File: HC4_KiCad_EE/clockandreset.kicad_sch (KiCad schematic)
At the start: 19 parts, among them IC15 74HC14, SW3 SW_Push, SW4 SW_Push, SW5 SW_SPDT, SW6 SW_SPDT

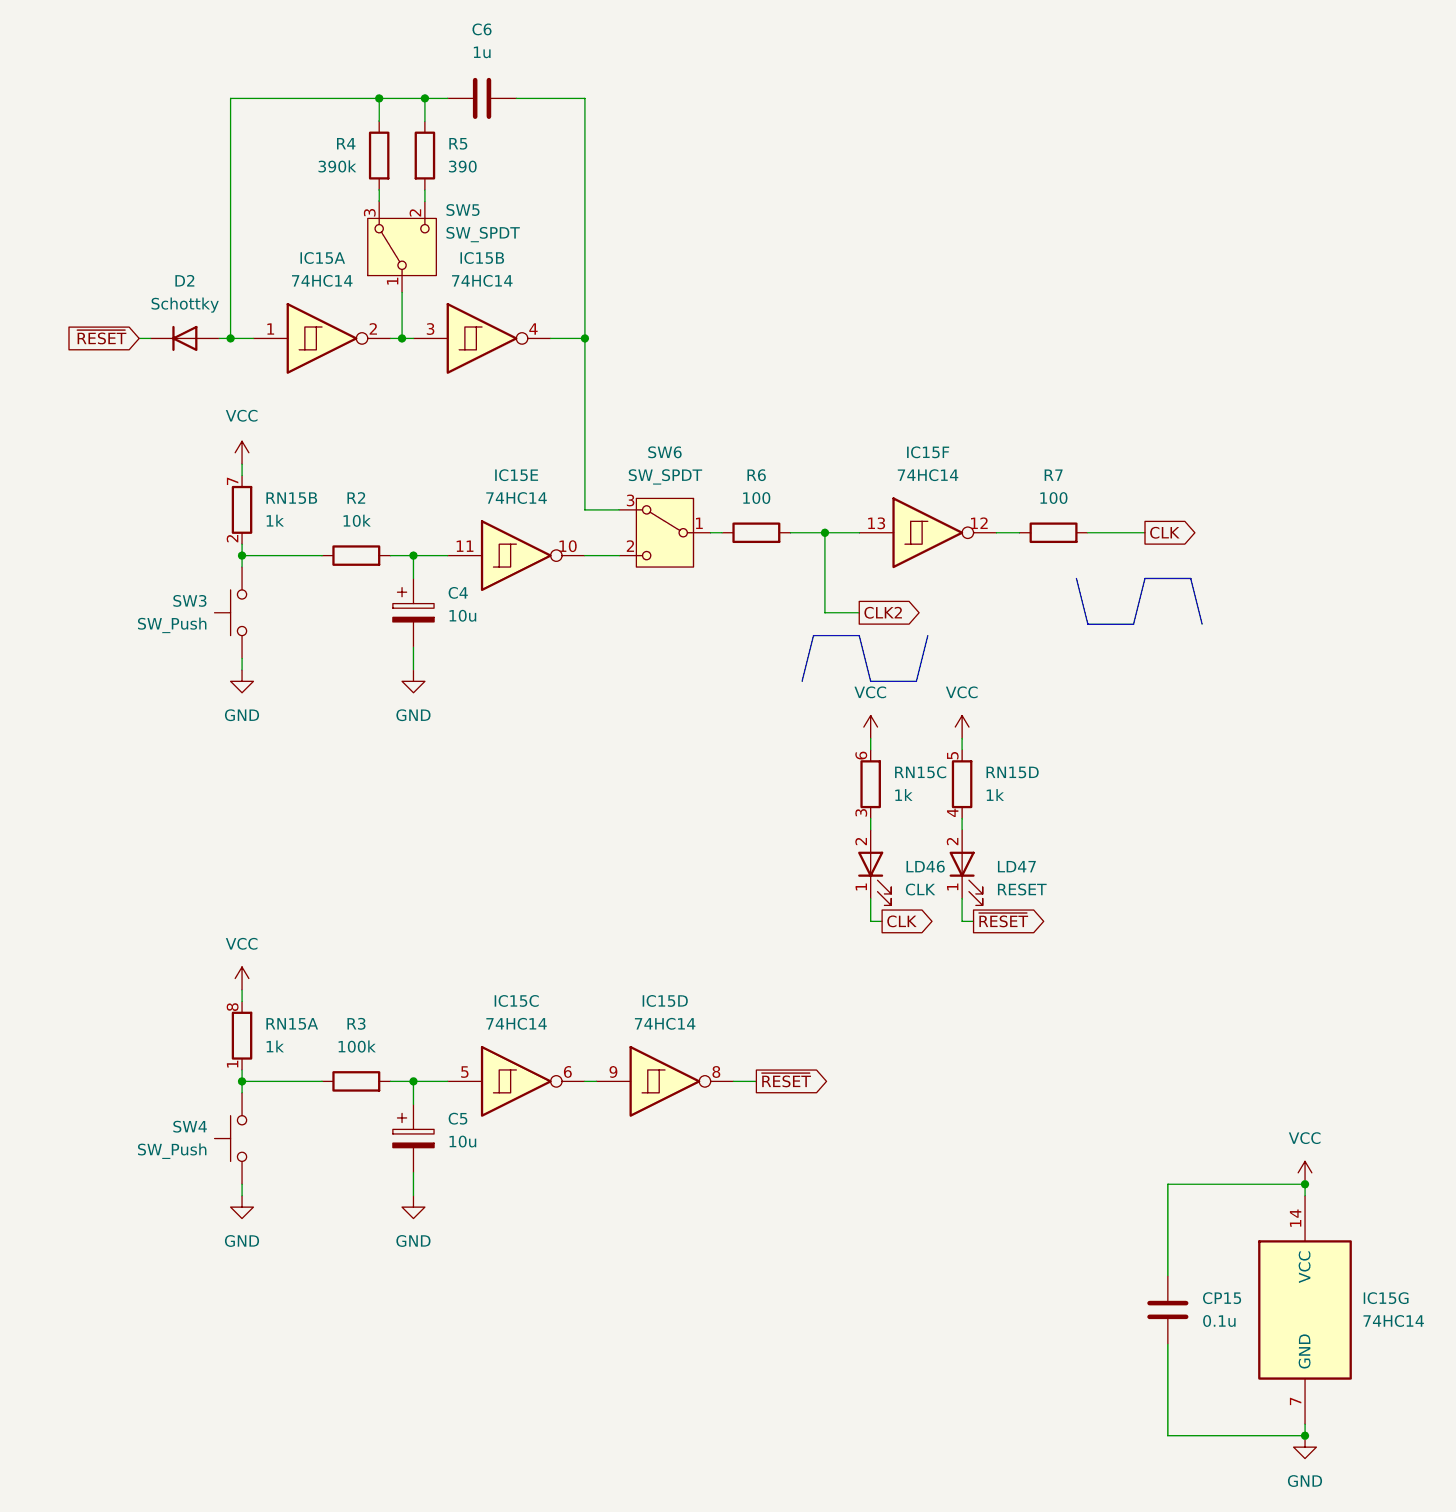
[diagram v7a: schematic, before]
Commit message: 基板を若干改版、フットプリントの指定が外れていたのを修正
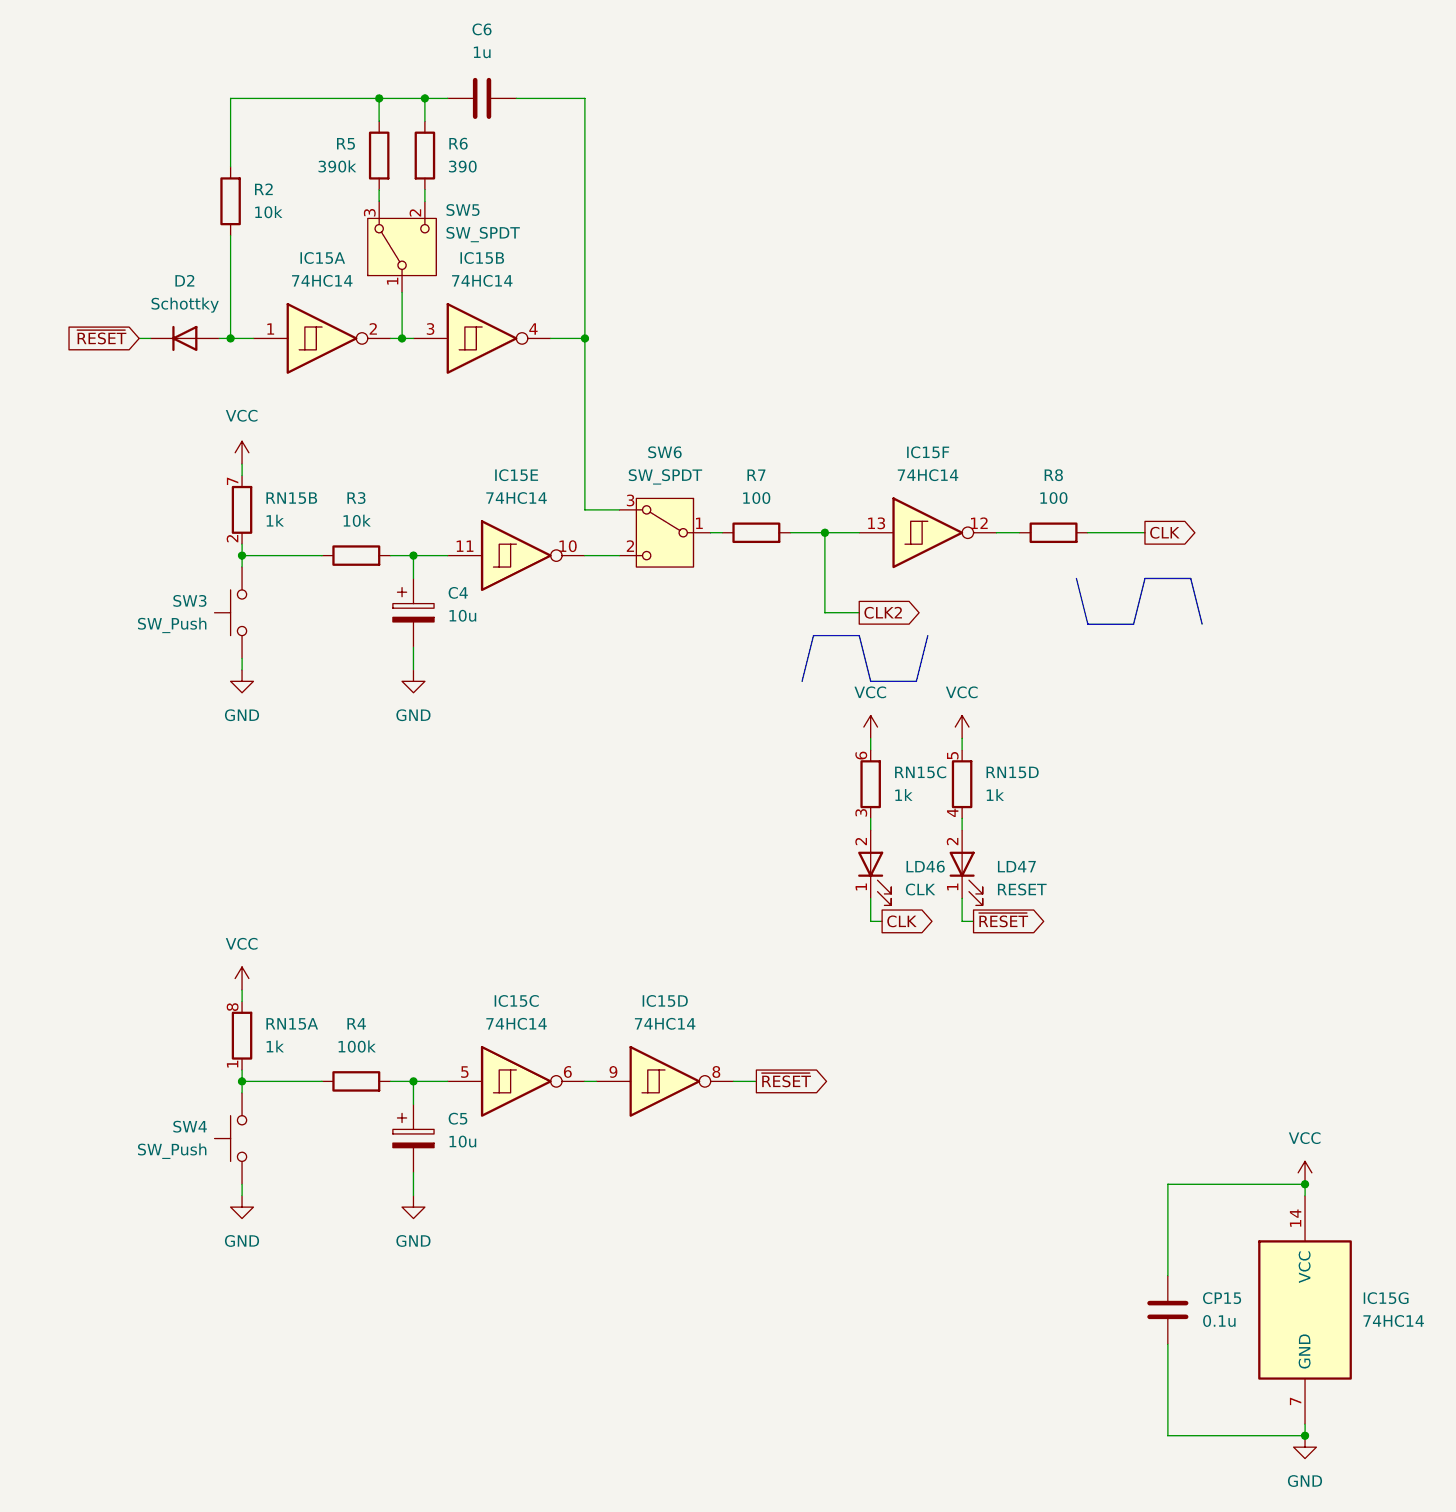
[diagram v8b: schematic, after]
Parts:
- added R2: 10k, Resistor_SMD:R_0603_1608Metric, symbol Device:R
- CP15: LCSC PN (none) -> C14663
- R3: renamed from R2; LCSC PN (none) -> C25804
- R4: renamed from R3; LCSC PN (none) -> C25803
- R5: renamed from R4; LCSC PN (none) -> C23137
- R6: renamed from R5; LCSC PN (none) -> C23151
- R7: renamed from R6; LCSC PN (none) -> C22775
- R8: renamed from R7; LCSC PN (none) -> C22775
- RN15: LCSC PN (none) -> C20197
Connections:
- net at C6.1, R5.1, R6.1: now also R2.2; no longer D2.2 (A), IC15.1
- new net: D2.2 (A), IC15.1, R2.1
